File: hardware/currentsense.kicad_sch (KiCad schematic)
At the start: 7 parts, among them U701 ACS711KEXLT-15AB-T, U702 ACS711KEXLT-15AB-T, U703 ACS711KEXLT-15AB-T

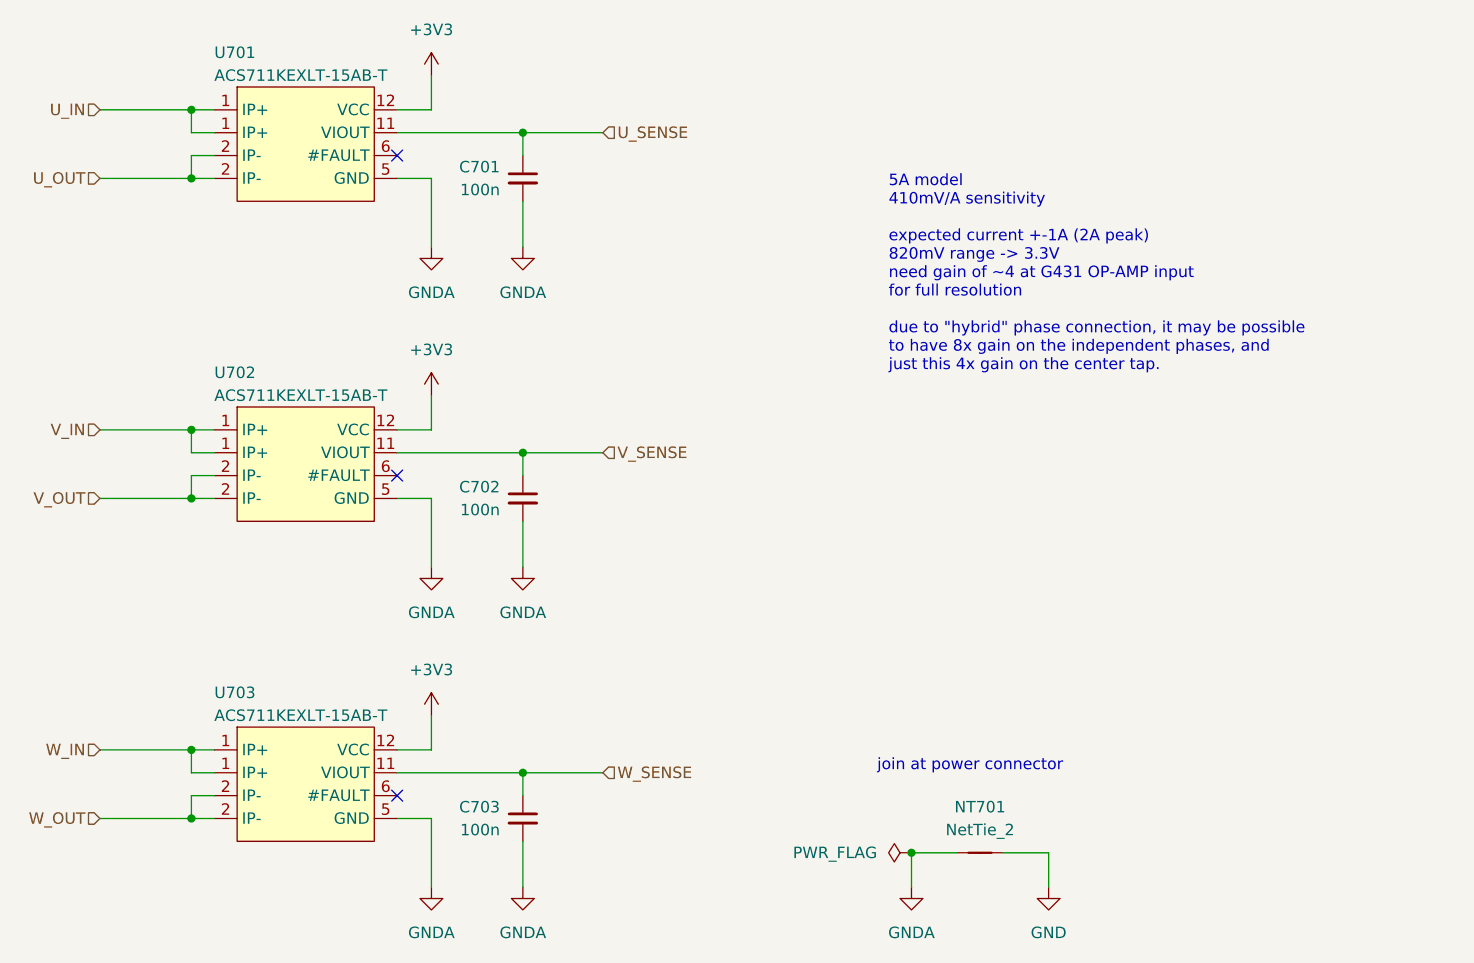
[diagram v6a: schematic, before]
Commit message: current sense LPF prototype
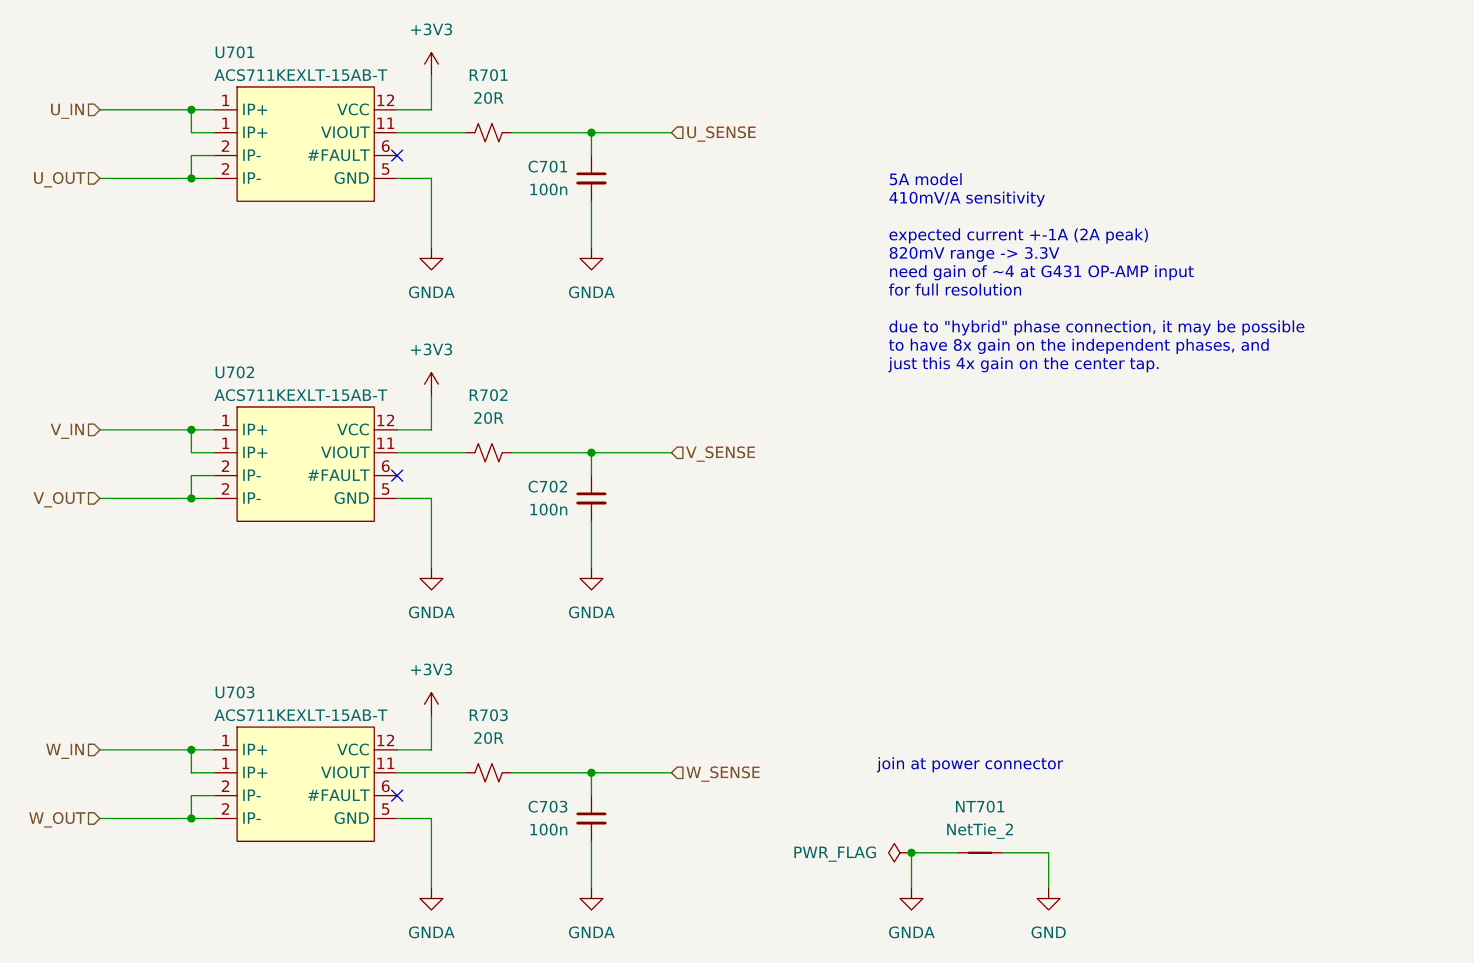
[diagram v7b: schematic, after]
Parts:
- added R701, R702, R703: 20R, Resistor_SMD:R_0402_1005Metric, symbol Device:R_Small_US
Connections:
- net U_SENSE: now also R701.2; no longer U701.11 (VIOUT)
- net V_SENSE: now also R702.2; no longer U702.11 (VIOUT)
- net W_SENSE: now also R703.2; no longer U703.11 (VIOUT)
- new net: R703.1, U703.11 (VIOUT)
- new net: R701.1, U701.11 (VIOUT)
- new net: R702.1, U702.11 (VIOUT)
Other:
- moved on the sheet: C701, C702, C703
